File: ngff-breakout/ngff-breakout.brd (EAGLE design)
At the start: 90 x 80 mm, 82 parts, among them U2 LD1085D2T33R, X1 PINHD-2X4, X3 694108106102, X8 ZX360D-B-10P(30), Y1 MHF4, Y2 MHF4, Y3 MHF4

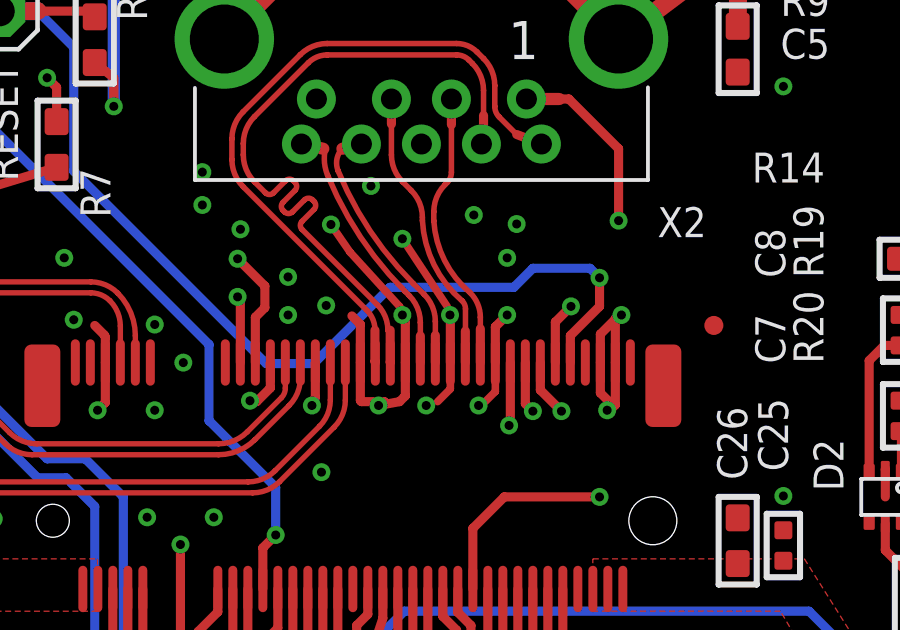
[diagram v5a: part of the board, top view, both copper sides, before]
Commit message: ngff: repair one critical via  for ERC passing
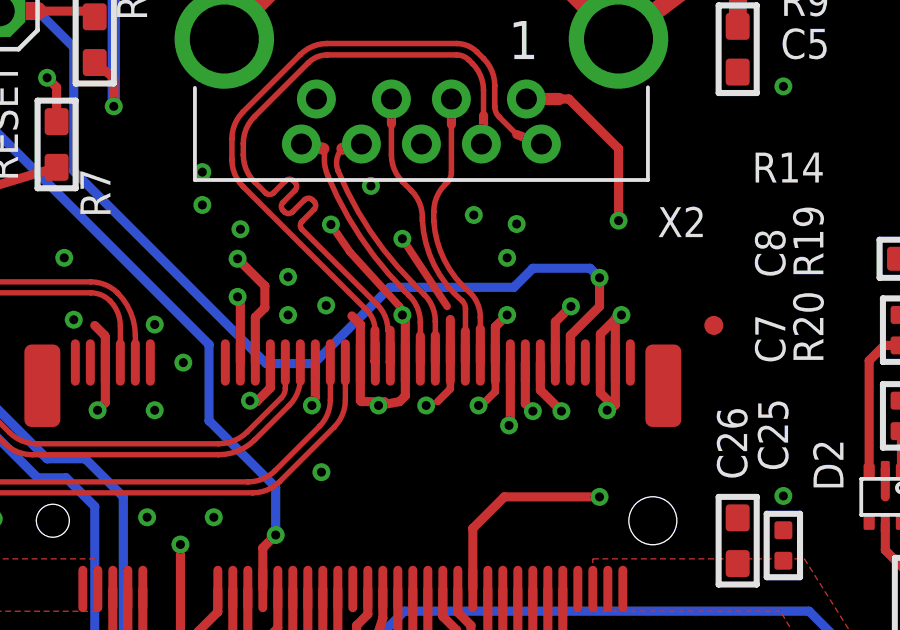
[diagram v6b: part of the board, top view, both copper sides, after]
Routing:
- net GND: vias 188 -> 187
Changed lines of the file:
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@@
 <contactref element="R14" pad="1"/>
 <wire x1="38.5125" y1="67.3405" x2="40.005" y2="65.0875" width="0.254" layer="1"/>
-<via x="40.1" y="64.8005" extent="1-16" drill="0.3"/>
 <via x="56.61" y="44.4805" extent="1-16" drill="0.3"/>
 </signal>

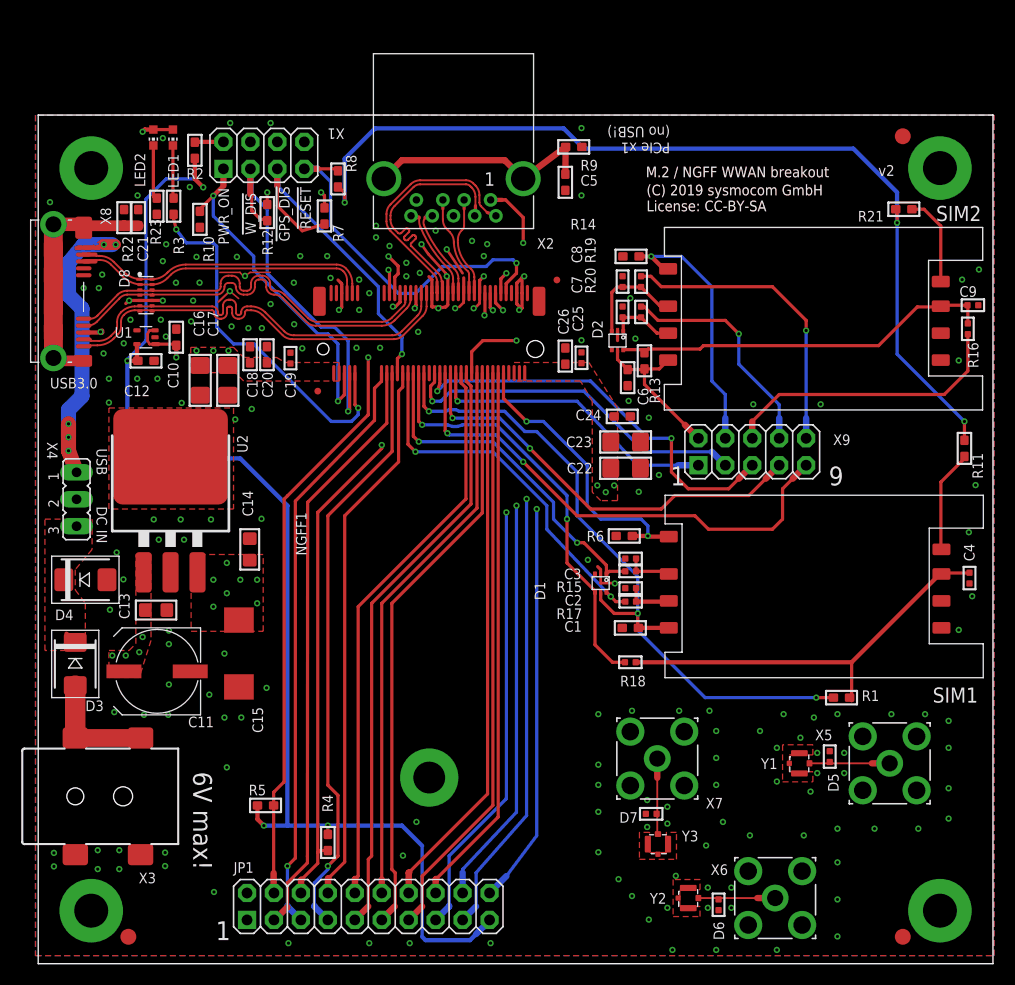
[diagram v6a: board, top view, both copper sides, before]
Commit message: ngff: re-introduce and re-position OSHW logo and bott silk screen
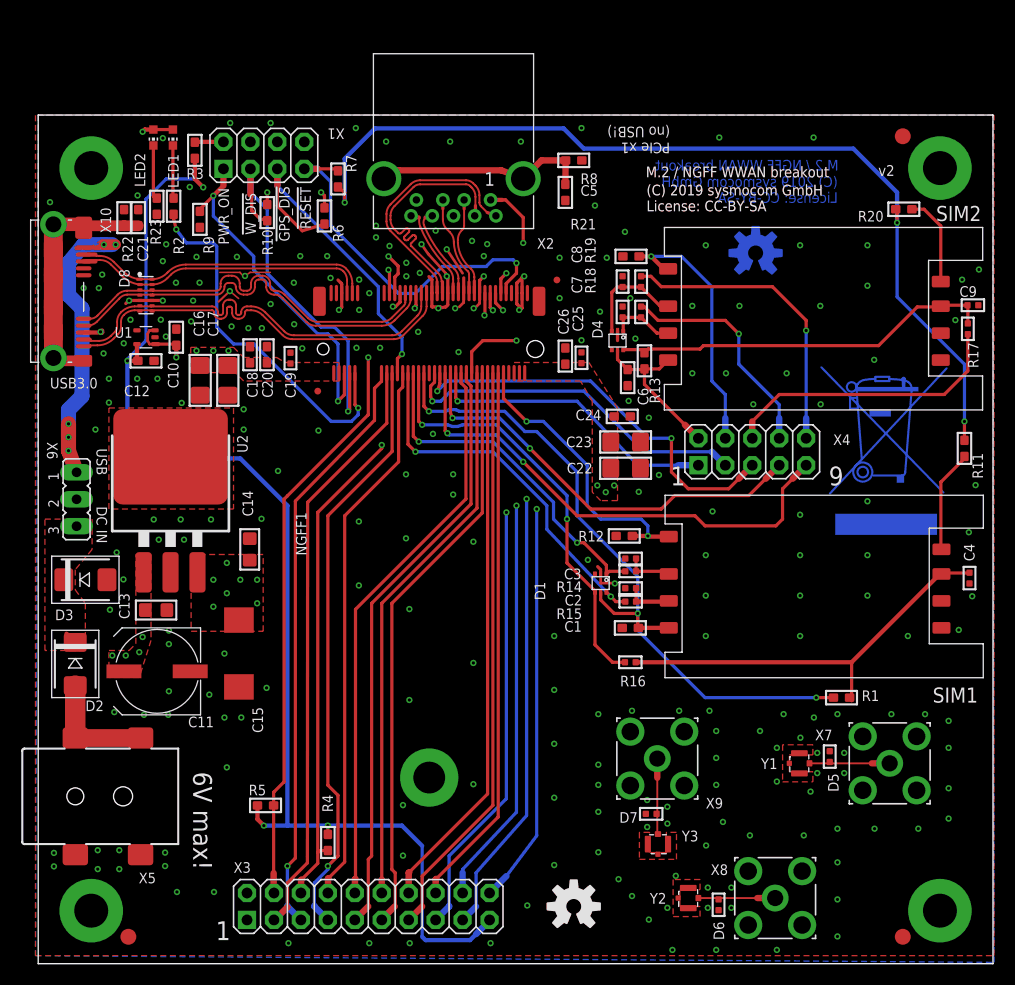
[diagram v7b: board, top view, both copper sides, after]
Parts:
- removed JP3: FIDUCIALUFIDUCIAL, SparkFun:MICRO-FIDUCIAL
- added U$1: (no value), laforge:WEEE_BIN_TOP
- added U$2: (no value), laforge:WEEE_BIN
- added U$3, U$5: (no value), SparkFun-Aesthetics:OSHW-LOGO-M_COPPER
- added U$4, U$6: (no value), SparkFun-Aesthetics:OSHW-LOGO-M
- added X10: ZX360D-B-10P(30), USB30-MICROB:ZX360D-B
- D2: value PESD5V0UBV -> SD2114S040S5R0; device laforge:SOT666 -> diodes-sysmocom:SMBDIODE
- D3: value SD2114S040S5R0 -> SMBJP6KE6.8A-TP
- D4: value SMBJP6KE6.8A-TP -> PESD5V0UBV; device diodes-sysmocom:SMBDIODE -> laforge:SOT666
- JP1: value (none) -> FIDUCIALUFIDUCIAL; device laforge:2X10 -> SparkFun:MICRO-FIDUCIAL
- R10: value 100k -> 10k
- R12: value 10k -> 47k
- R14: value 47k -> 47; device rc-sysmocom:_0603 -> rc-sysmocom:_0402
- R2, R8: value 10k -> 330
- R20: value 47 -> 4.7k; device rc-sysmocom:_0402 -> rc-sysmocom:_0603
- R21: value 4.7k -> 47k
- R3: value 330 -> 10k
- R6: value 47k -> 10k
- R9: value 330 -> 100k
- X3: value 694108106102 -> (none); device Wurth_Elektronik_Electromechanic_DC_Power_Jack_Connectors_rev15c:694108106102 -> laforge:2X10
- X4: device jumper:JP2 -> laforge:2X05
- X5: value (none) -> 694108106102; device laforge:SMA-F-S-TH -> Wurth_Elektronik_Electromechanic_DC_Power_Jack_Connectors_rev15c:694108106102
- X6: device laforge:SMA-F-S-TH -> jumper:JP2
- X8: value ZX360D-B-10P(30) -> (none); device USB30-MICROB:ZX360D-B -> laforge:SMA-F-S-TH
- X9: device laforge:2X05 -> laforge:SMA-F-S-TH
- moved X8 88.6 mm to (69.5, 6.19), turned to 180 degrees
- moved X5 81.8 mm to (-1.50, 15.8), turned to 0 degrees
- moved X6 75.8 mm to (3.62, 43.8), turned to 270 degrees
- moved X4 63.8 mm to (67.3, 48.3), turned to 0 degrees
- moved JP1 61.7 mm to (48.9, 64.5)
- moved D2 59.5 mm to (3.49, 28.3), turned to 270 degrees
- moved D4 55.0 mm to (54.6, 58.7), turned to 180 degrees
- moved R12 45.4 mm to (55.2, 40.3), turned to 0 degrees
- moved R16 44.7 mm to (55.8, 28.4), turned to 0 degrees
- moved R6 41.3 mm to (27.0, 70.5), turned to 90 degrees
- moved R17 40.9 mm to (87.6, 59.8), turned to 90 degrees
- moved R9 35.9 mm to (15.2, 70.2), turned to 90 degrees
- moved X3 34.2 mm to (31.1, 5.40)
- moved R18 33.0 mm to (56.8, 61.4), turned to 270 degrees
- moved X9 30.3 mm to (58.4, 19.3), turned to 180 degrees
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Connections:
- net !BODY_SAR: now also X3.4; no longer JP1.4
- net !CLKREQ: now also X3.9; no longer JP1.9
- net !GPS_DISABLE: now also R6.1; no longer R7.1
- net !PERST: now also X3.10; no longer JP1.10
- net !RESET: now also R7.1; no longer R8.1
- net !USIM1_RESET: now also R15.2; no longer R17.2
- net !USIM2_RESET: now also D4.1, R18.2; no longer D2.1, R20.2
- net !WAKE_ON_WWAN: now also X3.6; no longer JP1.6
- net !W_DISABLE: now also R10.1; no longer R12.1
- net ANTCTL0: now also X3.15; no longer JP1.15
- net ANTCTL1: now also X3.18; no longer JP1.18
- net ANTCTL2: now also X3.17; no longer JP1.17
- net ANTCTL3: now also X3.20; no longer JP1.20
- net COEX1: now also X3.16; no longer JP1.16
- net COEX2: now also X3.13; no longer JP1.13
- net COEX3: now also X3.14; no longer JP1.14
- net GND: now also D3.A, D4.2, R12.1, R21.1, R8.1, X10.5, X10.8, X5.2, X5.3, X8.G1, X8.G2, X8.G3, X8.G4, X9.G1, X9.G2, X9.G3, X9.G4; no longer D2.2, D4.A, JP1.2, R10.1, R14.1, R6.1, X3.3, X5.G1, X5.G2, X5.G3, X5.G4, X6.G1, X6.G2, X6.G3, X6.G4, X8.5, X8.8
- net LDO_IN: now also X6.2; no longer X4.2
- net N$10: now also X10.S1, X10.S2, X10.S3, X10.S4, X10.S5, X10.S6, X10.S7, X10.S8; no longer X8.S1, X8.S2, X8.S3, X8.S4, X8.S5, X8.S6, X8.S7, X8.S8
- net N$11: now also R20.2; no longer R21.2
- net N$12: now also D2.C, X6.3; no longer D4.C, X4.3
- net N$13: now also X7.C; no longer X5.C
- net N$14: now also X8.C; no longer X6.C
- net N$15: now also R17.1, X4.6; no longer R16.1, X9.6
- net N$16: now also R18.1, X4.8; no longer R20.1, X9.8
- net N$17: now also X10.4; no longer X8.4
- net N$18: now also R3.1; no longer R2.1
- net N$19: now also X4.10; no longer X9.10
- net N$2: now also R2.1; no longer R3.1
- net N$3: now also D2.A, X5.1, X5.1-1; no longer D3.A, X3.1, X3.1-1
- net N$4: now also R8.2; no longer R9.2
- net N$6: now also R2.2; no longer R3.2
- net N$7: now also X9.C; no longer X7.C
- net PCM_CLK: now also X3.5; no longer JP1.5
- net PCM_DIN: now also X3.3; no longer JP1.3
- net PCM_DOUT: now also X3.7; no longer JP1.7
- net PCM_SYNC: now also X3.8; no longer JP1.8
- net PWR_ON: now also R9.2; no longer R10.2
- net SIM1_DET: now also R12.2; no longer R6.2
- net SIM2_DET: now also R21.2, X4.4; no longer R14.2, X9.4
- net SMB_CLK: now also X3.11; no longer JP1.11
- net SMB_DATA: now also X3.12; no longer JP1.12
- net USB3.0_RX_N: now also X10.9; no longer X8.9
- net USB3.0_RX_P: now also X10.10; no longer X8.10
- net USB3.0_TX_N: now also X10.6; no longer X8.6
- net USB3.0_TX_P: now also X10.7; no longer X8.7
- net USB_VBUS: now also X10.1, X6.1; no longer X4.1, X8.1
- net USIM1_CLK: now also R14.2; no longer R15.2
- net USIM1_DATA: now also R16.2; no longer R18.2
- net USIM2_CLK: now also D4.3; no longer D2.3
- net USIM2_DATA: now also D4.6, R17.2; no longer D2.6, R16.2
- net USIM2_POWER: now also D4.5, X4.2; no longer D2.5, X9.2
- net VCC_1V8: now also R10.2, R20.1, R3.2, R6.2, X3.19; no longer JP1.19, R12.2, R2.2, R21.1, R8.2
- net VCC_3V3: now also X3.1; no longer JP1.1
- net _!USIM1_RESET: now also R15.1; no longer R17.1
- net _!USIM2_RESET: now also X4.7; no longer X9.7
- net _SIM2_DET: now also X4.3; no longer X9.3
- net _USB_D_N: now also X10.2; no longer X8.2
- net _USB_D_P: now also X10.3; no longer X8.3
- net _USIM1_CLK: now also R14.1; no longer R15.1
- net _USIM1_DATA: now also R16.1; no longer R18.1
- net _USIM2_CLK: now also X4.9; no longer X9.9
- net _USIM2_DATA: now also X4.5; no longer X9.5
- net _USIM2_POWER: now also X4.1; no longer X9.1
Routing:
- net N$4: track 22.2 -> 20.5 mm
- net GND: vias 187 -> 244
